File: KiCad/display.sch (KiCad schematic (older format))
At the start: 72 parts, among them IC11 SN74LV1T125DCKR, IC6 PCA9517ADP, J1 46756-1001, J2 2129320-3, T1 BSS138APW

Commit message: Changed package of SN74LV1T125 to SOT32
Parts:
- added U11: SN74LV1T125DBVR, antmicro-footprints:SOT-23-5, symbol antmicroLogicBuffersDriversReceiversTransceivers:SN74LV1T125DBVR
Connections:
- wire segments 268 -> 270
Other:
- moved on the sheet: C5, IC11
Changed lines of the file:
@@
-$EndComp
-$Comp
-L jetson-nano-baseboard:GND #GND_0141
-U 1 1 5E7104BB
-P 10500 9475
-F 0 "#GND_0141" H 10500 9475 20  0001 C CNN
-F 1 "GND" H 10502 9328 30  0000 C CNN
-F 2 "" H 10500 9475 70  0001 C CNN
-F 3 "" H 10500 9475 70  0001 C CNN
-	1    10500 9475
-	1    0    0    -1
 $EndComp
 $Comp
@@
 $EndComp
 $Comp
-L jetson-nano-baseboard:SN74LV1T125 IC11
-U 1 1 5E7104AA
-P 9900 9250
-F 0 "IC11" H 10198 9603 60  0000 R BNN
-F 1 "SN74LV1T125DCKR" H 10198 9478 60  0000 R BNN
-F 2 "jetson-nano-baseboard-footprints:SC70-5" H 10200 9450 60  0001 C CNN
-F 3 "" H 10200 9450 60  0001 C CNN
-F 4 "Texas Instrumets" V 2300 1957 60  0001 C CNN "Manufacturer"
-F 5 "SN74LV1T125DCKR" H -14198 -15753 50  0001 C CNN "MPN"
-	1    9900 9250
-	-1   0    0    -1
-$EndComp
-$Comp
 L jetson-nano-baseboard:BLM18SG121TN1D L10
 U 1 1 5E7104AB
@@
 F 5 "BLM18SG121TN1D" H -14648 -15078 50  0001 C CNN "MPN"
 	1    6650 6725
-	1    0    0    -1
-$EndComp
-$Comp
-L jetson-nano-baseboard:miniDP J2
-U 1 1 5E7104B2
-P 6775 8300
-F 0 "J2" H 6075 9400 60  0000 L BNN
-F 1 "2129320-3" H 6077 9253 60  0000 L BNN
-F 2 "jetson-nano-baseboard-footprints:2129320-3" H 6075 9200 60  0001 C CNN
-F 3 "" H 6075 9200 60  0001 C CNN
-F 4 "TE" V 1875 2607 60  0001 C CNN "Manufacturer"
-F 5 "2309413-1" H -14623 -15103 50  0001 C CNN "MPN"
-	1    6775 8300
 	1    0    0    -1
 $EndComp
@@
 L jetson-nano-baseboard:GND #GND_0142
 U 1 1 5E7104BA
-P 9325 9725
-F 0 "#GND_0142" H 9325 9725 20  0001 C CNN
-F 1 "GND" H 9327 9578 30  0000 C CNN
-F 2 "" H 9325 9725 70  0001 C CNN
-F 3 "" H 9325 9725 70  0001 C CNN
-	1    9325 9725
+P 9325 8975
+F 0 "#GND_0142" H 9325 8975 20  0001 C CNN
+F 1 "GND" H 9327 8828 30  0000 C CNN
+F 2 "" H 9325 8975 70  0001 C CNN
+F 3 "" H 9325 8975 70  0001 C CNN
+	1    9325 8975
 	1    0    0    -1
 $EndComp
@@
 Text GLabel 9175 7500 2    50   Input ~ 0
 DP_PWR
-Text GLabel 9325 8900 1    50   Input ~ 0
+Text GLabel 9325 8575 1    50   Input ~ 0
 1V8_SYS
 Text GLabel 4675 10250 2    50   Input ~ 0
@@
 Text GLabel 6375 6725 0    50   Input ~ 0
 3V3_SYS
-Text Label 8700 9350 0    60   ~ 0
+Text Label 8700 9250 0    60   ~ 0
 DP_HPD
 Text Label 8175 7700 2    60   ~ 0
@@
 Wire Wire Line
 	12150 8550 12450 8550
-Wire Wire Line
-	9400 9350 8700 9350
-Wire Wire Line
-	10400 9150 10500 9150
-Wire Wire Line
-	10500 9150 10500 9350
-Wire Wire Line
-	10400 9350 10500 9350
-Connection ~ 10500 9350
-Wire Wire Line
-	10500 9350 10500 9475
 Text Label 11500 9250 2    60   ~ 0
 DP_HPD_IN
@@
 Wire Wire Line
 	11250 9250 11500 9250
-Wire Wire Line
-	9400 9150 9325 9150
 Wire Wire Line
 	6450 6725 6375 6725
@@
 L jetson-nano-baseboard:C_100n_0402 C5
 U 1 1 615EE274
-P 9325 9550
-F 0 "C5" H 9475 9600 60  0000 C CNN
-F 1 "C_100n_0402" H 9325 9400 60  0001 C CNN
-F 2 "jetson-nano-baseboard-footprints:0402-cap" H 9525 9750 60  0001 L CNN
-F 3 "" H 9325 9550 50  0001 C CNN
-F 4 "Walsin" H 9525 9950 60  0001 L CNN "Manufacturer"
-F 5 "0402X104K6R3CT" H 9525 9850 60  0001 L CNN "MPN"
-F 6 "100n" H 9500 9500 50  0000 C CNN "Val"
-	1    9325 9550
-	1    0    0    -1
-$EndComp
-Wire Wire Line
-	9325 8900 9325 9150
-Connection ~ 9325 9150
-Wire Wire Line
-	9325 9150 9325 9400
-Wire Wire Line
-	9325 9700 9325 9725
+P 9325 8800
+F 0 "C5" H 9475 8850 60  0000 C CNN
+F 1 "C_100n_0402" H 9325 8650 60  0001 C CNN
+F 2 "jetson-nano-baseboard-footprints:0402-cap" H 9525 9000 60  0001 L CNN
+F 3 "" H 9325 8800 50  0001 C CNN
+F 4 "Walsin" H 9525 9200 60  0001 L CNN "Manufacturer"
+F 5 "0402X104K6R3CT" H 9525 9100 60  0001 L CNN "MPN"
+F 6 "100n" H 9500 8750 50  0000 C CNN "Val"
+	1    9325 8800
+	1    0    0    -1
+$EndComp
+Wire Wire Line
+	9325 8950 9325 8975
 $Comp
 L jetson-nano-baseboard:R_100k_0402 R100
@@
 $EndComp
 Wire Wire Line
-	10400 9250 10700 9250
-Wire Wire Line
 	10700 9300 10700 9250
-Connection ~ 10700 9250
 Wire Wire Line
 	10700 9250 11250 9250
@@
 	1    0    0    -1
 $EndComp
+$Comp
+L antmicroLogicBuffersDriversReceiversTransceivers:SN74LV1T125DBVR U11
+U 1 1 6163A187
+P 9875 9150
+F 0 "U11" H 9700 9525 60  0000 C CNN
+F 1 "SN74LV1T125DBVR" H 9325 9425 60  0000 C CNN
+F 2 "antmicro-footprints:SOT-23-5" H 10075 9350 60  0001 L CNN
+F 3 "https://www.ti.com/lit/ds/symlink/sn74lv1t125.pdf?HQS=dis-mous-null-mousermode-dsf-pf-null-wwe&ts=1627648952184&ref_url=https%253A%252F%252Fpl.mouser.com%252F" H 10075 9450 60  0001 L CNN
+F 4 "SN74LV1T125DBVR" H 10075 9650 60  0001 L CNN "MPN"
+F 5 "Texas Instruments" H 10075 10250 60  0001 L CNN "Manufacturer"
+	1    9875 9150
+	-1   0    0    -1
+$EndComp
+$Comp
+L jetson-nano-baseboard:SN74LV1T125 IC11
+U 1 1 5E7104AA
+P 9925 10400
+F 0 "IC11" H 10223 10753 60  0000 R BNN
+F 1 "SN74LV1T125DCKR" H 10223 10628 60  0000 R BNN
+F 2 "jetson-nano-baseboard-footprints:SC70-5" H 10225 10600 60  0001 C CNN
+F 3 "" H 10225 10600 60  0001 C CNN
+F 4 "Texas Instrumets" V 2325 3107 60  0001 C CNN "Manufacturer"
+F 5 "SN74LV1T125DCKR" H -14173 -14603 50  0001 C CNN "MPN"
+	1    9925 10400
+	-1   0    0    -1
+$EndComp
+Wire Wire Line
+	9325 8575 9325 8600
+Wire Wire Line
+	8700 9250 9675 9250
+Wire Wire Line
+	9325 8600 9875 8600
+Wire Wire Line
+	9875 8600 9875 8850
+Connection ~ 9325 8600
+Wire Wire Line
+	9325 8600 9325 8650
+Wire Wire Line
+	9875 9450 9875 9475
+$Comp
+L jetson-nano-baseboard:GND #GND_0141
+U 1 1 6176A9D0
+P 9875 9525
+F 0 "#GND_0141" H 9875 9525 20  0001 C CNN
+F 1 "GND" H 9877 9378 30  0000 C CNN
+F 2 "" H 9875 9525 70  0001 C CNN
+F 3 "" H 9875 9525 70  0001 C CNN
+	1    9875 9525
+	1    0    0    -1
+$EndComp
+Wire Wire Line
+	10175 9250 10700 9250
+Connection ~ 10700 9250
+Wire Wire Line
+	10175 9050 10250 9050
+Wire Wire Line
+	10250 9050 10250 9475
+Wire Wire Line
+	10250 9475 9875 9475
+Connection ~ 9875 9475
+Wire Wire Line
+	9875 9475 9875 9525
+$Comp
+L jetson-nano-baseboard:miniDP J2
+U 1 1 5E7104B2
+P 6775 8300
+F 0 "J2" H 6075 9400 60  0000 L BNN
+F 1 "2129320-3" H 6077 9253 60  0000 L BNN
+F 2 "jetson-nano-baseboard-footprints:2129320-3" H 6075 9200 60  0001 C CNN
+F 3 "" H 6075 9200 60  0001 C CNN
+F 4 "TE" V 1875 2607 60  0001 C CNN "Manufacturer"
+F 5 "2309413-1" H -14623 -15103 50  0001 C CNN "MPN"
+	1    6775 8300
+	1    0    0    -1
+$EndComp

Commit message: Changed DP connector to micro HDMI on schematic
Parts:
- removed C3, C4: C_4u7_0402, jetson-nano-baseboard-footprints:0402-cap, symbol jetson-nano-baseboard:C_4u7_0402
- removed C44, C45, C5: C_100n_0402, jetson-nano-baseboard-footprints:0402-cap, symbol jetson-nano-baseboard:C_100n_0402
- removed D12: TPD2E009DBZR, jetson-nano-baseboard-footprints:SOT-23s, symbol jetson-nano-baseboard:TPD2E009
- removed D2: 1N4148WS, jetson-nano-baseboard-footprints:SOD-323, symbol jetson-nano-baseboard:diode
- removed IC11: SN74LV1T125DCKR, jetson-nano-baseboard-footprints:SC70-5, symbol jetson-nano-baseboard:SN74LV1T125
- removed J2: 2129320-3, jetson-nano-baseboard-footprints:2129320-3, symbol jetson-nano-baseboard:miniDP
- removed L10: BLM18SG121TN1D, jetson-nano-baseboard-footprints:0603, symbol jetson-nano-baseboard:BLM18SG121TN1D
- removed R100, R26, R30: R_100k_0402, jetson-nano-baseboard-footprints:0402-res, symbol jetson-nano-baseboard:R_100k_0402
- removed R31, R32: R_1M0_0402, jetson-nano-baseboard-footprints:0402-res, symbol jetson-nano-baseboard:R_1M0_0402
- removed U11: SN74LV1T125DBVR, antmicro-footprints:SOT-23-5, symbol antmicroLogicBuffersDriversReceiversTransceivers:SN74LV1T125DBVR
- added C? (x2): C_4u7_0402, jetson-nano-baseboard-footprints:0402-cap, symbol jetson-nano-baseboard:C_4u7_0402
- added C? (x2): C_100n_0402, jetson-nano-baseboard-footprints:0402-cap, symbol jetson-nano-baseboard:C_100n_0402
- added D?: 1N4148WS, jetson-nano-baseboard-footprints:SOD-323, symbol jetson-nano-baseboard:diode
- added D? (x2): TPD2E009DBZR, jetson-nano-baseboard-footprints:SOT-23s, symbol jetson-nano-baseboard:TPD2E009
- added IC?: PCA9517ADP, jetson-nano-baseboard-footprints:MSOP-8, symbol jetson-nano-baseboard:PCA9517ADP
- added J?: 46756-1001, antmicro-footprints:HDMI_Micro-D_Molex_46765-1x01, symbol antmicroUSBDVIHDMIConnectors:46756-1001
- added L? (x2): BLM18SG121TN1D, jetson-nano-baseboard-footprints:0603, symbol jetson-nano-baseboard:BLM18SG121TN1D
- added R? (x4): R_0R_0402, jetson-nano-baseboard-footprints:0402-res, symbol jetson-nano-baseboard:R_0R_0402
- added R? (x7): R_2k_0402, jetson-nano-baseboard-footprints:0402-res, symbol jetson-nano-baseboard:R_2k_0402
- added R? (x8): R_5R6_0402, jetson-nano-baseboard-footprints:0402-res, symbol jetson-nano-baseboard:R_5R6_0402
- added T?: BSS138APW, jetson-nano-baseboard-footprints:SC70-3, symbol jetson-nano-baseboard:BSS138APW
- added TP? (x2): ~, jetson-nano-baseboard-footprints:TP-R-1.5, symbol jetson-nano-baseboard:Testpad
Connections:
- net labels removed: DP_CEC, DP_HPD_IN, DP_MODE, DP_PWR, EDP_C_AUX_C_N, EDP_C_AUX_C_P
- wire segments 270 -> 316
- no-connect marks 3 -> 4
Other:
- note removed: "DisplayPort Interface"
- moved on the sheet: C1, C12, C2, C26, C27, C39, C40, C42, C43, C6, C7, C73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

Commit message: Change TPD2E009DBZR with PESD2USB5UV-TR on schematic
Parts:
- removed C? (x2): C_4u7_0402, jetson-nano-baseboard-footprints:0402-cap, symbol jetson-nano-baseboard:C_4u7_0402
- removed C? (x2): C_100n_0402, jetson-nano-baseboard-footprints:0402-cap, symbol jetson-nano-baseboard:C_100n_0402
- removed D10, D11, D? (x2): TPD2E009DBZR, jetson-nano-baseboard-footprints:SOT-23s, symbol jetson-nano-baseboard:TPD2E009
- removed D?: 1N4148WS, jetson-nano-baseboard-footprints:SOD-323, symbol jetson-nano-baseboard:diode
- removed IC?: PCA9517ADP, jetson-nano-baseboard-footprints:MSOP-8, symbol jetson-nano-baseboard:PCA9517ADP
- removed J?: 46756-1001, antmicro-footprints:HDMI_Micro-D_Molex_46765-1x01, symbol antmicroUSBDVIHDMIConnectors:46756-1001
- removed L? (x2): BLM18SG121TN1D, jetson-nano-baseboard-footprints:0603, symbol jetson-nano-baseboard:BLM18SG121TN1D
- removed R? (x4): R_0R_0402, jetson-nano-baseboard-footprints:0402-res, symbol jetson-nano-baseboard:R_0R_0402
- removed R? (x7): R_2k_0402, jetson-nano-baseboard-footprints:0402-res, symbol jetson-nano-baseboard:R_2k_0402
- removed R? (x8): R_5R6_0402, jetson-nano-baseboard-footprints:0402-res, symbol jetson-nano-baseboard:R_5R6_0402
- removed T?: BSS138APW, jetson-nano-baseboard-footprints:SC70-3, symbol jetson-nano-baseboard:BSS138APW
- removed TP? (x2): ~, jetson-nano-baseboard-footprints:TP-R-1.5, symbol jetson-nano-baseboard:Testpad
- added C3, C4: C_4u7_0402, jetson-nano-baseboard-footprints:0402-cap, symbol jetson-nano-baseboard:C_4u7_0402
- added C44, C45, C5: C_100n_0402, jetson-nano-baseboard-footprints:0402-cap, symbol jetson-nano-baseboard:C_100n_0402
- added D10, D11, D12: PESD2USB5UV-TR, antmicro-footprints:SOT-23s, symbol antmicroTVSDiodes:PESD2USB5UV-TR
- added D2: 1N4148WS, jetson-nano-baseboard-footprints:SOD-323, symbol jetson-nano-baseboard:diode
- added IC11: SN74LV1T125DBVR, antmicro-footprints:SOT-23-5, symbol antmicroLogicBuffersDriversReceiversTransceivers:SN74LV1T125DBVR
- added J2: 2129320-3, jetson-nano-baseboard-footprints:2129320-3, symbol jetson-nano-baseboard:miniDP
- added L10: BLM18SG121TN1D, jetson-nano-baseboard-footprints:0603, symbol jetson-nano-baseboard:BLM18SG121TN1D
- added R100, R26, R30: R_100k_0402, jetson-nano-baseboard-footprints:0402-res, symbol jetson-nano-baseboard:R_100k_0402
- added R31, R32: R_1M0_0402, jetson-nano-baseboard-footprints:0402-res, symbol jetson-nano-baseboard:R_1M0_0402
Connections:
- net labels added: DP_CEC, DP_HPD_IN, DP_MODE, DP_PWR, EDP_C_AUX_C_N, EDP_C_AUX_C_P
- wire segments 316 -> 270
- no-connect marks 4 -> 3
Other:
- note added: "DisplayPort Interface"
- moved on the sheet: C1, C12, C2, C26, C27, C39, C40, C42, C43, C6, C7, C73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

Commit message: Move ethernet connector closet to the edge. Loclib
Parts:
- D10, D11, D12: footprint antmicro-footprints:SOT-23s -> jetson-nano-baseboard-footprints:SOT-23s; symbol antmicroTVSDiodes:PESD2USB5UV-TR -> jetson-nano-baseboard:PESD2USB5UV-TR
- IC11: footprint antmicro-footprints:SOT-23-5 -> jetson-nano-baseboard-footprints:SOT-23-5; symbol antmicroLogicBuffersDriversReceiversTransceivers:SN74LV1T125DBVR -> jetson-nano-baseboard:SN74LV1T125DBVR
- J1: footprint antmicro-footprints:HDMI_Micro-D_Molex_46765-1x01 -> jetson-nano-baseboard-footprints:HDMI_Micro-D_Molex_46765-1x01; symbol antmicroUSBDVIHDMIConnectors:46756-1001 -> jetson-nano-baseboard:46756-1001
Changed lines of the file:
@@
 DisplayPort Interface
 $Comp
-L antmicroUSBDVIHDMIConnectors:46756-1001 J1
+L jetson-nano-baseboard:46756-1001 J1
 U 1 1 616F319B
 P 14350 2825
 F 0 "J1" H 14780 2962 50  0000 L CNN
 F 1 "46756-1001" H 14780 2871 50  0000 L CNN
-F 2 "antmicro-footprints:HDMI_Micro-D_Molex_46765-1x01" H 14350 2825 50  0001 C CNN
+F 2 "jetson-nano-baseboard-footprints:HDMI_Micro-D_Molex_46765-1x01" H 14350 2825 50  0001 C CNN
 F 3 "https://www.molex.com/webdocs/datasheets/pdf/en-us/0467651001_IO_CONNECTORS.pdf" H 14350 2825 50  0001 C CNN
 F 4 "467651001" H 14780 2780 50  0000 L CNN "MPN"
@@
 Connection ~ 10700 9250
 $Comp
-L antmicroLogicBuffersDriversReceiversTransceivers:SN74LV1T125DBVR IC11
+L jetson-nano-baseboard:SN74LV1T125DBVR IC11
 U 1 1 6163A187
 P 9875 9150
 F 0 "IC11" H 9700 9525 60  0000 C CNN
 F 1 "SN74LV1T125DBVR" H 9325 9425 60  0000 C CNN
-F 2 "antmicro-footprints:SOT-23-5" H 10075 9350 60  0001 L CNN
+F 2 "jetson-nano-baseboard-footprints:SOT-23-5" H 10075 9350 60  0001 L CNN
 F 3 "https://www.ti.com/lit/ds/symlink/sn74lv1t125.pdf?HQS=dis-mous-null-mousermode-dsf-pf-null-wwe&ts=1627648952184&ref_url=https%253A%252F%252Fpl.mouser.com%252F" H 10075 9450 60  0001 L CNN
 F 4 "SN74LV1T125DBVR" H 10075 9650 60  0001 L CNN "MPN"
@@
 Connection ~ 9875 9475
 $Comp
-L antmicroTVSDiodes:PESD2USB5UV-TR D?
+L jetson-nano-baseboard:PESD2USB5UV-TR D?
 U 1 1 61CAA79F
 P 14475 7300
@@
 F 0 "D10" V 14515 7430 60  0000 L CNN
 F 1 "PESD2USB5UV-TR" V 14621 7430 60  0000 L CNN
-F 2 "antmicro-footprints:SOT-23s" H 14525 7500 60  0001 C CNN
+F 2 "jetson-nano-baseboard-footprints:SOT-23s" H 14525 7500 60  0001 C CNN
 F 3 "https://assets.nexperia.com/documents/data-sheet/PESD2USB5UV-T.pdf" H 14475 7300 60  0001 C CNN
 F 4 "PESD2USB5UV-TR " H 14175 7600 50  0001 C CNN "MPN"
@@
 $EndComp
 $Comp
-L antmicroTVSDiodes:PESD2USB5UV-TR D?
+L jetson-nano-baseboard:PESD2USB5UV-TR D?
 U 1 1 61CC12F9
 P 14025 9275
@@
 F 0 "D11" V 14065 9405 60  0000 L CNN
 F 1 "PESD2USB5UV-TR" V 14171 9405 60  0000 L CNN
-F 2 "antmicro-footprints:SOT-23s" H 14075 9475 60  0001 C CNN
+F 2 "jetson-nano-baseboard-footprints:SOT-23s" H 14075 9475 60  0001 C CNN
 F 3 "https://assets.nexperia.com/documents/data-sheet/PESD2USB5UV-T.pdf" H 14025 9275 60  0001 C CNN
 F 4 "PESD2USB5UV-TR " H 13725 9575 50  0001 C CNN "MPN"
@@
 $EndComp
 $Comp
-L antmicroTVSDiodes:PESD2USB5UV-TR D?
+L jetson-nano-baseboard:PESD2USB5UV-TR D?
 U 1 1 61CD7958
 P 11350 9775
@@
 F 0 "D12" V 11390 9905 60  0000 L CNN
 F 1 "PESD2USB5UV-TR" V 11496 9905 60  0000 L CNN
-F 2 "antmicro-footprints:SOT-23s" H 11400 9975 60  0001 C CNN
+F 2 "jetson-nano-baseboard-footprints:SOT-23s" H 11400 9975 60  0001 C CNN
 F 3 "https://assets.nexperia.com/documents/data-sheet/PESD2USB5UV-T.pdf" H 11350 9775 60  0001 C CNN
 F 4 "PESD2USB5UV-TR " H 11050 10075 50  0001 C CNN "MPN"

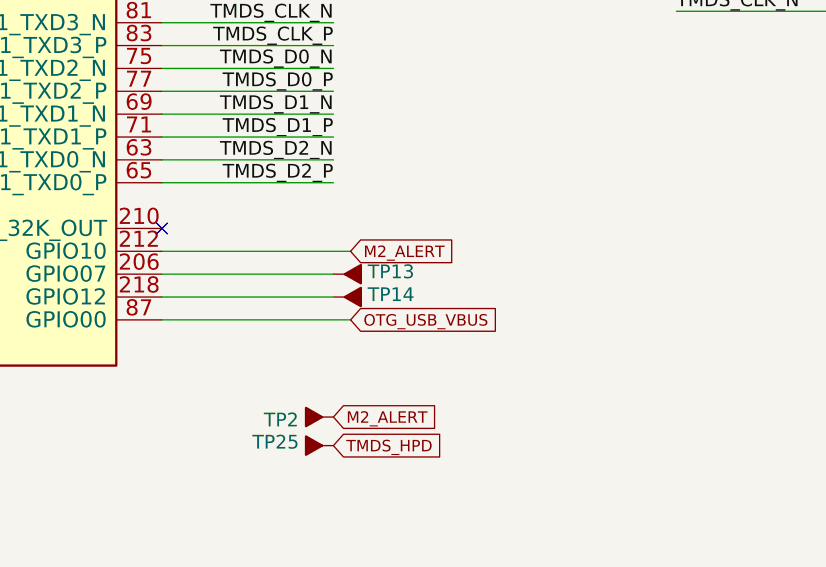
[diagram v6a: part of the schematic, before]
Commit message: Change fan design to match Nvidia. Change user button and led pins
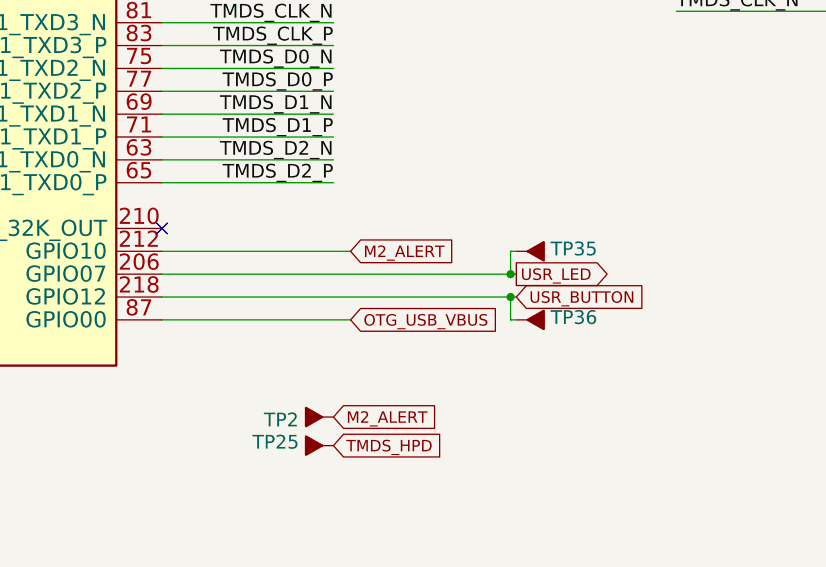
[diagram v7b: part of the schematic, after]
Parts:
- renumbered TP13 to TP35, TP14 to TP36
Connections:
- net USR_LED: now reaches M1.206 (GPIO07), TP35.1 (P)
- net USR_BUTTON: now reaches M1.218 (GPIO12), TP36.1 (P)
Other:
- moved on the sheet: TP35, TP36
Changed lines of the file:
@@
 	0    -1   -1   0
-$EndComp
-$Comp
-L jetson-nano-baseboard:Testpad TP13
-U 1 1 5E7104A6
-P 3300 4600
-F 0 "TP13" V 3325 4700 60  0000 L BNN
-F 1 "~" H 3300 4600 50  0001 C CNN
-F 2 "jetson-nano-baseboard-footprints:TP-R-1.5" H 3300 4600 50  0001 C CNN
-F 3 "" H 3300 4600 50  0001 C CNN
-F 4 "N/A" H -14148 -15703 50  0001 C CNN "MPN"
-F 5 "N/A" H -14148 -15703 50  0001 C CNN "Manufacturer"
-	1    3300 4600
-	0    1    1    0
-$EndComp
-$Comp
-L jetson-nano-baseboard:Testpad TP14
-U 1 1 5E7104A7
-P 3300 4700
-F 0 "TP14" V 3325 4800 60  0000 L BNN
-F 1 "~" H 3300 4700 50  0001 C CNN
-F 2 "jetson-nano-baseboard-footprints:TP-R-1.5" H 3300 4700 50  0001 C CNN
-F 3 "" H 3300 4700 50  0001 C CNN
-F 4 "N/A" H -14148 -15703 50  0001 C CNN "MPN"
-F 5 "N/A" H -14148 -15703 50  0001 C CNN "Manufacturer"
-	1    3300 4700
-	0    1    1    0
 $EndComp
 Text Label 890  5140 0    70   ~ 0
@@
 	2500 4200 3250 4200
 Wire Wire Line
-	2500 4600 3250 4600
-Wire Wire Line
-	2500 4700 3250 4700
-Wire Wire Line
 	2500 4800 3325 4800
 NoConn ~ 2500 4400
@@
 	0    1    1    0
 $EndComp
+$Comp
+L jetson-nano-baseboard:Testpad TP35
+U 1 1 5E7104A6
+P 4100 4500
+F 0 "TP35" V 4125 4600 60  0000 L BNN
+F 1 "~" H 4100 4500 50  0001 C CNN
+F 2 "jetson-nano-baseboard-footprints:TP-R-1.5" H 4100 4500 50  0001 C CNN
+F 3 "" H 4100 4500 50  0001 C CNN
+F 4 "N/A" H -13348 -15803 50  0001 C CNN "MPN"
+F 5 "N/A" H -13348 -15803 50  0001 C CNN "Manufacturer"
+	1    4100 4500
+	0    1    1    0
+$EndComp
+$Comp
+L jetson-nano-baseboard:Testpad TP36
+U 1 1 5E7104A7
+P 4100 4800
+F 0 "TP36" V 4125 4900 60  0000 L BNN
+F 1 "~" H 4100 4800 50  0001 C CNN
+F 2 "jetson-nano-baseboard-footprints:TP-R-1.5" H 4100 4800 50  0001 C CNN
+F 3 "" H 4100 4800 50  0001 C CNN
+F 4 "N/A" H -13348 -15603 50  0001 C CNN "MPN"
+F 5 "N/A" H -13348 -15603 50  0001 C CNN "Manufacturer"
+	1    4100 4800
+	0    1    1    0
+$EndComp
+Text GLabel 4050 4600 2    50   Output ~ 0
+USR_LED
+Text GLabel 4050 4700 2    50   Input ~ 0
+USR_BUTTON
+Wire Wire Line
+	4050 4500 4025 4500
+Wire Wire Line
+	4025 4500 4025 4600
+Wire Wire Line
+	4025 4600 4050 4600
+Wire Wire Line
+	4050 4800 4025 4800
+Wire Wire Line
+	4025 4800 4025 4700
+Wire Wire Line
+	4025 4700 4050 4700
+Wire Wire Line
+	2500 4700 4025 4700
+Connection ~ 4025 4700
+Wire Wire Line
+	2500 4600 4025 4600
+Connection ~ 4025 4600
 $EndSCHEMATC
